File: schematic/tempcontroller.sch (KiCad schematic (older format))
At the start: 3 parts

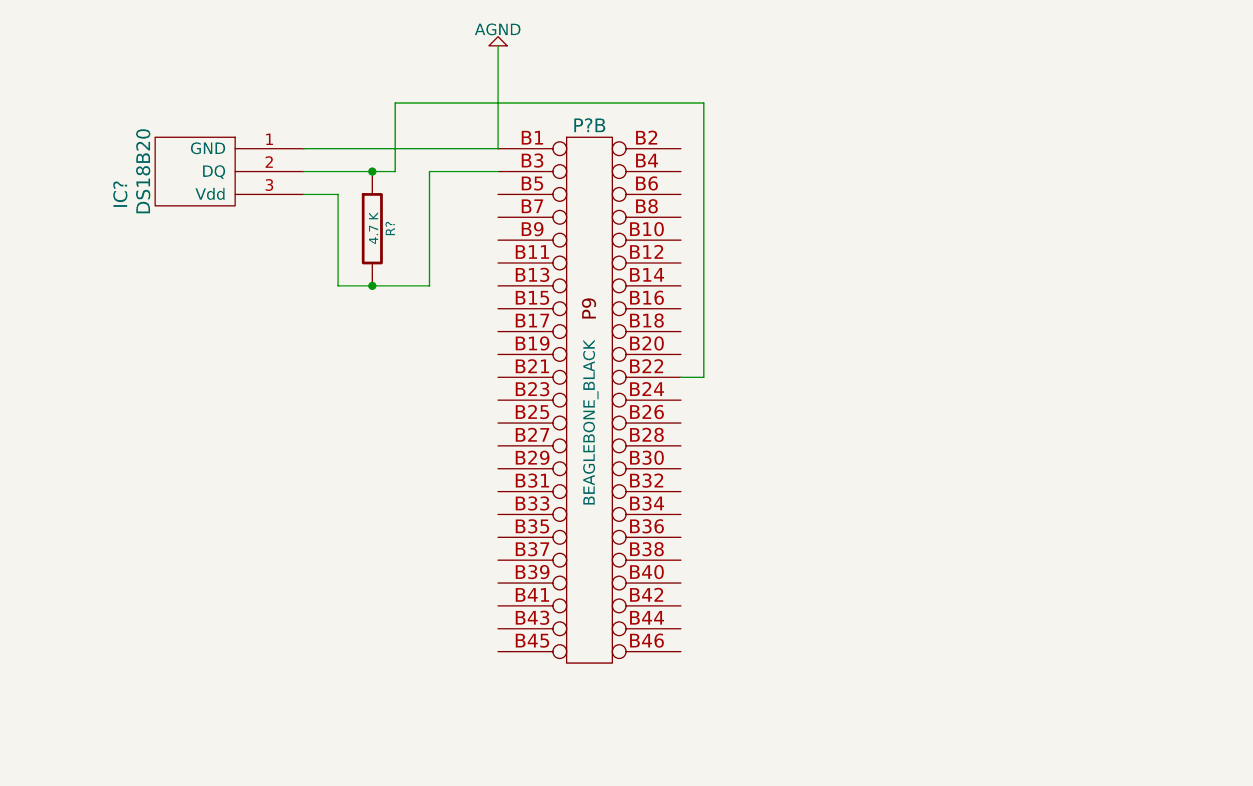
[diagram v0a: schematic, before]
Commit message: added led
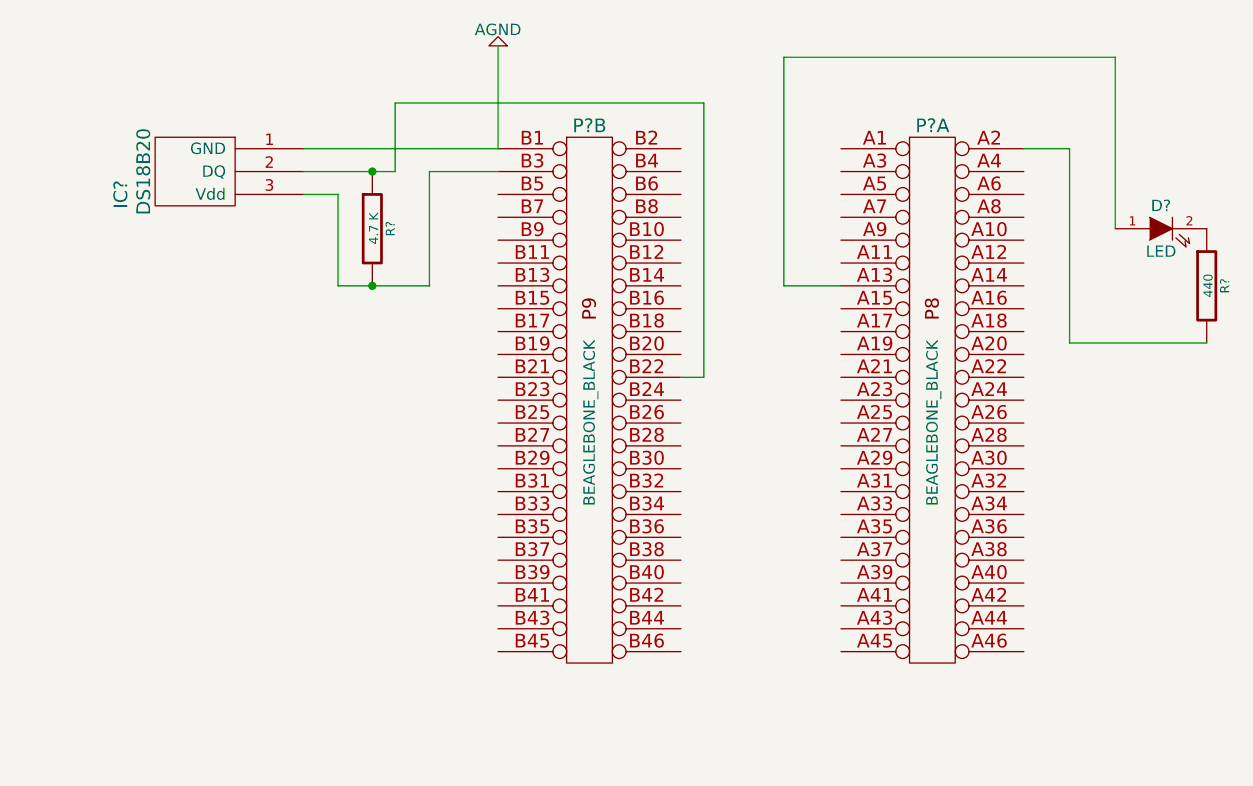
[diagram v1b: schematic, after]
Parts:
- added D?: LED, ~, symbol LED
- added P?: BEAGLEBONE_BLACK, ~, symbol BEAGLEBONE_BLACK
- added R?: 440, ~, symbol R
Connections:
- new net: D?.1 (A), P?.A13 (P13)
- new net: P?.A2 (P2), R?.2
- new net: D?.2 (K), R?.1
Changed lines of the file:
@@
 LIBS:boneheaderlib
 LIBS:beagleboard
+LIBS:tempcontroller-cache
+LIBS:tempcontroller-cache
 EELAYER 27 0
 EELAYER END
@@
 Sheet 1 1
 Title "noname.sch"
-Date "8 feb 2015"
+Date "20 dec 2015"
 Rev ""
 Comp ""
@@
 $EndComp
 Wire Wire Line
-	2250 2150 2550 2150
-Wire Wire Line
-	2550 2150 2650 2150
+	2250 2150 2650 2150
 Wire Wire Line
 	2650 2150 2650 1850
@@
 	2400 2250 2400 2650
 Wire Wire Line
-	2400 2650 2550 2650
-Wire Wire Line
-	2550 2650 2800 2650
+	2400 2650 2800 2650
 Wire Wire Line
 	2800 2650 2800 2150
@@
 Wire Wire Line
 	3100 2050 3100 1600
+$Comp
+L BEAGLEBONE_BLACK P?
+U 1 1 56771C91
+P 5000 3250
+F 0 "P?" H 5000 4550 60  0000 C CNN
+F 1 "BEAGLEBONE_BLACK" V 5000 3250 50  0000 C CNN
+F 2 "~" H 5000 3250 60  0000 C CNN
+F 3 "~" H 5000 3250 60  0000 C CNN
+	1    5000 3250
+	1    0    0    -1
+$EndComp
+$Comp
+L LED D?
+U 1 1 56771CDA
+P 6000 2400
+F 0 "D?" H 6000 2500 50  0000 C CNN
+F 1 "LED" H 6000 2300 50  0000 C CNN
+F 2 "~" H 6000 2400 60  0000 C CNN
+F 3 "~" H 6000 2400 60  0000 C CNN
+	1    6000 2400
+	1    0    0    -1
+$EndComp
+$Comp
+L R R?
+U 1 1 56771D88
+P 6200 2650
+F 0 "R?" V 6280 2650 40  0000 C CNN
+F 1 "440" V 6207 2651 40  0000 C CNN
+F 2 "~" V 6130 2650 30  0000 C CNN
+F 3 "~" H 6200 2650 30  0000 C CNN
+	1    6200 2650
+	1    0    0    -1
+$EndComp
+Wire Wire Line
+	4600 2650 4350 2650
+Wire Wire Line
+	4350 2650 4350 1650
+Wire Wire Line
+	4350 1650 5800 1650
+Wire Wire Line
+	5800 1650 5800 2400
+Wire Wire Line
+	6200 2900 5600 2900
+Wire Wire Line
+	5600 2900 5600 2050
+Wire Wire Line
+	5600 2050 5400 2050
 $EndSCHEMATC

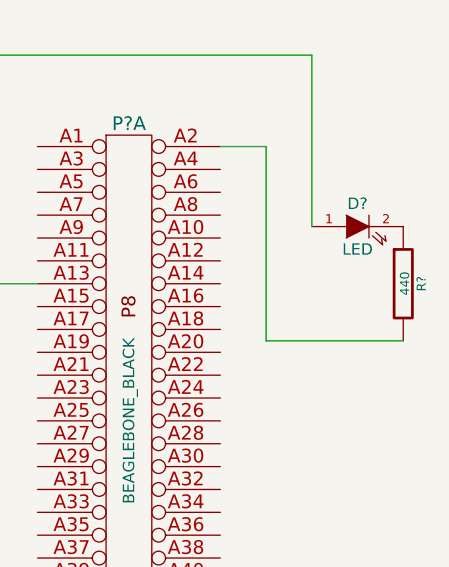
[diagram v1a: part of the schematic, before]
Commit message: update resistor value for led
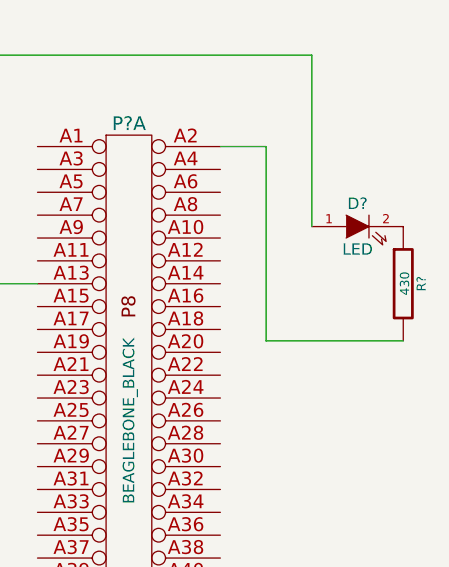
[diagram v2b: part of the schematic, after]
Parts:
- R?: value 440 -> 430
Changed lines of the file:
@@
 Sheet 1 1
 Title "noname.sch"
-Date "20 dec 2015"
+Date "21 dec 2015"
 Rev ""
 Comp ""
@@
 P 6200 2650
 F 0 "R?" V 6280 2650 40  0000 C CNN
-F 1 "440" V 6207 2651 40  0000 C CNN
+F 1 "430" V 6207 2651 40  0000 C CNN
 F 2 "~" V 6130 2650 30  0000 C CNN
 F 3 "~" H 6200 2650 30  0000 C CNN

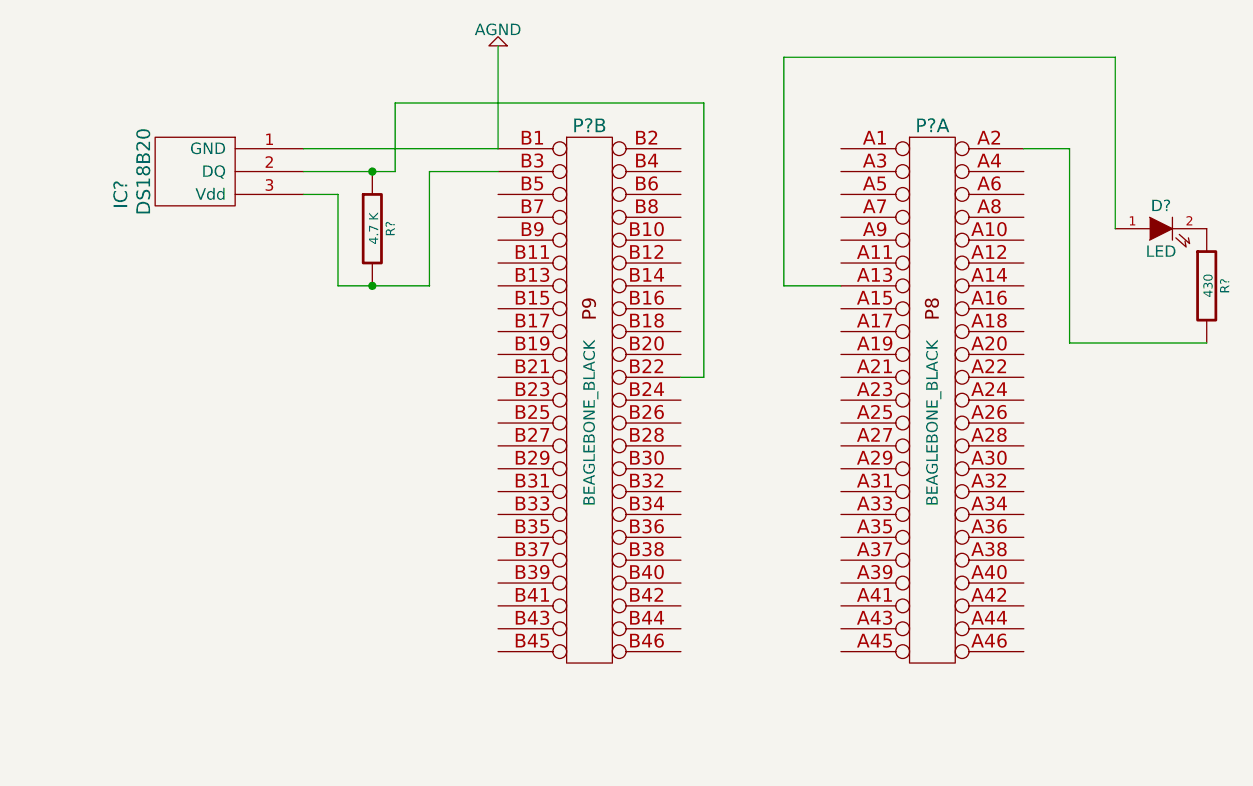
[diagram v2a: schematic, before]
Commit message: added ambient temperature sensor
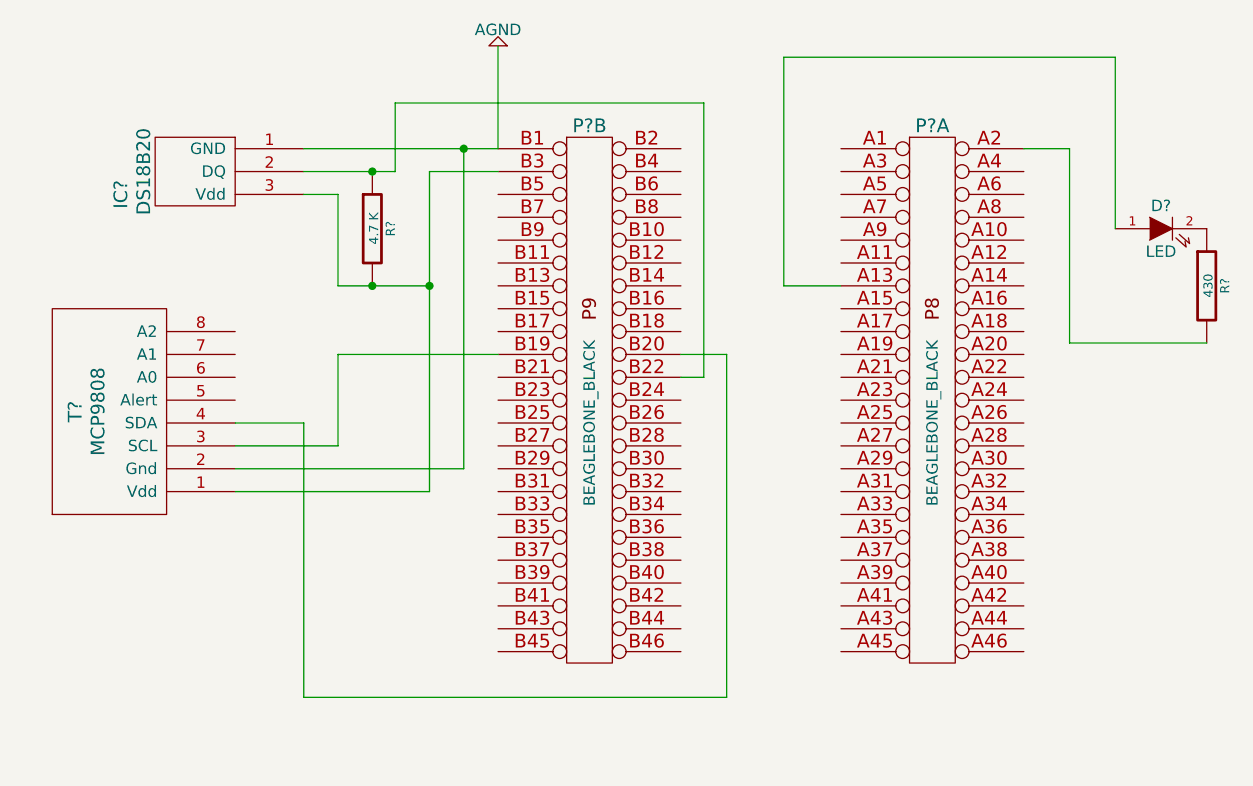
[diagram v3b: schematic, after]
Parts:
- added T?: MCP9808, symbol MCP9808
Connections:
- net AGND: now also T?.2 (Gnd)
- net at IC?.3 (Vdd), P?.B3, R?.2: now also T?.1 (Vdd)
- net at P?.B19 (P19): now also T?.3 (SCL)
- net at P?.B20 (P20): now also T?.4 (SDA)
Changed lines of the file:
@@
 Sheet 1 1
 Title "noname.sch"
-Date "21 dec 2015"
+Date "10 jan 2016"
 Rev ""
 Comp ""
@@
 $EndComp
 Wire Wire Line
-	2250 2150 2650 2150
+	2250 2150 2550 2150
+Wire Wire Line
+	2550 2150 2650 2150
 Wire Wire Line
 	2650 2150 2650 1850
@@
 	2400 2250 2400 2650
 Wire Wire Line
-	2400 2650 2800 2650
+	2400 2650 2550 2650
 Wire Wire Line
-	2800 2650 2800 2150
+	2550 2650 2800 2650
+Wire Wire Line
+	2800 2150 2800 2650
+Wire Wire Line
+	2800 2650 2800 3550
 Wire Wire Line
 	2800 2150 3100 2150
 Connection ~ 2550 2650
 Wire Wire Line
-	2250 2050 3100 2050
+	2250 2050 2950 2050
+Wire Wire Line
+	2950 2050 3100 2050
 $Comp
 L AGND #PWR?
@@
 Wire Wire Line
 	5600 2050 5400 2050
+$Comp
+L MCP9808 T?
+U 1 1 569276C4
+P 1250 3200
+F 0 "T?" H 1250 3200 60  0000 C CNN
+F 1 "MCP9808" H 1250 3100 60  0000 C CNN
+F 2 "" H 1250 3200 60  0000 C CNN
+F 3 "" H 1250 3200 60  0000 C CNN
+	1    1250 3200
+	0    -1   -1   0
+$EndComp
+Wire Wire Line
+	2800 3550 1950 3550
+Connection ~ 2800 2650
+Wire Wire Line
+	2950 2050 2950 3450
+Wire Wire Line
+	2950 3450 1950 3450
+Connection ~ 2950 2050
+Wire Wire Line
+	3100 2950 2400 2950
+Wire Wire Line
+	2400 2950 2400 3350
+Wire Wire Line
+	2400 3350 1950 3350
+Wire Wire Line
+	3900 2950 4100 2950
+Wire Wire Line
+	4100 2950 4100 4450
+Wire Wire Line
+	4100 4450 2250 4450
+Wire Wire Line
+	2250 3250 2250 4450
+Wire Wire Line
+	1950 3250 2250 3250
 $EndSCHEMATC

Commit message: add display
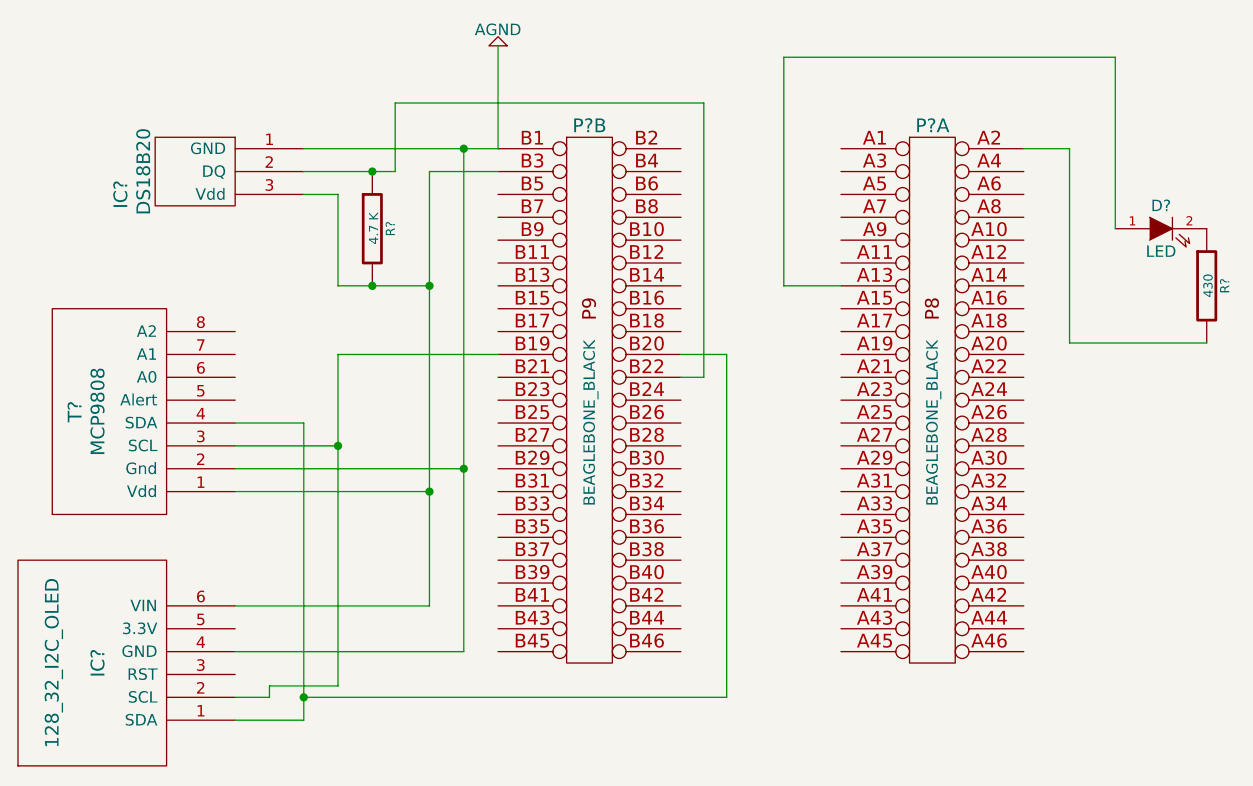
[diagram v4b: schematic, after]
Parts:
- added IC?: 128_32_I2C_OLED, symbol 128_32_I2C_OLED
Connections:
- net AGND: now also IC?.4 (GND)
- net at IC?.3 (Vdd), P?.B3, R?.2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: now also IC?.6 (VIN)
- net at P?.B19 (P19), T?.3 (SCL): now also IC?.2 (SCL)
- net at P?.B20 (P20), T?.4 (SDA): now also IC?.1 (SDA)
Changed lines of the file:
@@
 Sheet 1 1
 Title "noname.sch"
-Date "10 jan 2016"
+Date "19 jan 2016"
 Rev ""
 Comp ""
@@
 $EndComp
 Wire Wire Line
-	2250 2150 2550 2150
-Wire Wire Line
-	2550 2150 2650 2150
+	2250 2150 2650 2150
 Wire Wire Line
 	2650 2150 2650 1850
@@
 	2400 2250 2400 2650
 Wire Wire Line
-	2400 2650 2550 2650
+	2400 2650 2800 2650
 Wire Wire Line
-	2550 2650 2800 2650
-Wire Wire Line
-	2800 2150 2800 2650
-Wire Wire Line
-	2800 2650 2800 3550
+	2800 2150 2800 4050
 Wire Wire Line
 	2800 2150 3100 2150
 Connection ~ 2550 2650
 Wire Wire Line
-	2250 2050 2950 2050
-Wire Wire Line
-	2950 2050 3100 2050
+	2250 2050 3100 2050
 $Comp
 L AGND #PWR?
@@
 Connection ~ 2800 2650
 Wire Wire Line
-	2950 2050 2950 3450
+	2950 2050 2950 4250
 Wire Wire Line
 	2950 3450 1950 3450
@@
 	3100 2950 2400 2950
 Wire Wire Line
-	2400 2950 2400 3350
+	2400 2950 2400 4400
 Wire Wire Line
 	2400 3350 1950 3350
@@
 	4100 4450 2250 4450
 Wire Wire Line
-	2250 3250 2250 4450
+	2250 3250 2250 4550
 Wire Wire Line
-	1950 3250 2250 3250
+	2250 3250 1950 3250
+$Comp
+L 128_32_I2C_OLED IC?
+U 1 1 569D9CD1
+P 1300 4300
+F 0 "IC?" H 1300 4250 60  0000 C CNN
+F 1 "128_32_I2C_OLED" H 1300 4450 60  0000 C CNN
+F 2 "" H 1300 4150 60  0000 C CNN
+F 3 "" H 1300 4150 60  0000 C CNN
+	1    1300 4300
+	0    -1   -1   0
+$EndComp
+Wire Wire Line
+	2250 4550 1950 4550
+Connection ~ 2250 4450
+Wire Wire Line
+	2400 4400 2100 4400
+Wire Wire Line
+	2100 4400 2100 4450
+Wire Wire Line
+	2100 4450 1950 4450
+Connection ~ 2400 3350
+Wire Wire Line
+	2950 4250 1950 4250
+Connection ~ 2950 3450
+Wire Wire Line
+	2800 4050 1950 4050
+Connection ~ 2800 3550
 $EndSCHEMATC
